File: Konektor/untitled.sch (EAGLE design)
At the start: 13 parts, among them J1 1744429-4, J2 1744429-4, J4 1744429-2, J5 1744429-2, J6 1744429-2, X1 MSTBA2, X2 MSTBA4, X3 MSTBA6, X6 MSTBA2, X7 C-GRID-02-70543, X8 MSTBA2

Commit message: PCB huawei
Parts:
- removed J4, J5, J6: 1744429-2, 1744429-2:1744429-2
- J1, J2: value 1744429-4 -> RJ45-8N-B; device 1744429-4:1744429-4 -> RJ45-8N-B:RJ45-8N-B
- X2: value MSTBA4 -> MSTBA5; device con-phoenix-508:MSTBA4 -> con-phoenix-508:MSTBA5
- X3: value MSTBA6 -> MSTBA5; device con-phoenix-508:MSTBA6 -> con-phoenix-508:MSTBA5
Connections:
- new net N$19: J1.8, J2.8
- new net N$20: J1.SHIELD, J2.SHIELD
- new net N$7: X2-5.1, X3-1.1
- new net N$8: J1.1, J2.1
- net N$10: now also J1.3, J2.3; no longer J4.2, X3-2.1
- net N$11: now also J1.4, J2.4; no longer J5.1, X3-3.1
- net N$12: now also J1.5, J2.5; no longer J5.2, X3-4.1
- net N$13: now also J1.6, J2.6; no longer J6.1, X3-5.1
- net N$14: now also J1.7, J2.7; no longer J6.2, X3-6.1
- net N$3: now also X3-5.1; no longer J1.1
- net N$4: now also X3-4.1; no longer J1.3
- net N$5: now also X3-3.1; no longer J2.1
- net N$6: now also X3-2.1; no longer J2.3
- net N$9: now also J1.2, J2.2; no longer J4.1, X3-1.1
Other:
- note removed: "ARUS R S T"
- note removed: "TEGANGAN 3 Phase"
- moved on the sheet: S1, X2-1, X2-2, X2-3, X2-4, X3-1, X3-2, X3-3, X3-4, X3-5, X6-1, X6-2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

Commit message: 3 PCB done
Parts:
- removed S1: DS01-254-L-04BE, DS01-254-L-04BE:DS01-254-L-04BE
- removed X3: MSTBA5, con-phoenix-508:MSTBA5
- removed X6, X8: MSTBA2, con-phoenix-508:MSTBA2
- removed X7: C-GRID-02-70543, con-molex:C-GRID-02-70543
- added DP-05RP1: (no value), DP-05RP:DP-05RP
- added EBYTEE220-900T22D1: (no value), EByte E220-900T22D:EBYTEE220-900T22D
- added KONEKTOR-3.81-13P1: (no value), KONEKTOR-3.81-13P:KONEKTOR-3.81-13P
- added R1: 10k, rcl:R-EU_R0805
- added RS1: C-GRID-02-70543, con-molex:C-GRID-02-70543
- added TTL-RS1: (no value), TTL-RS485:TTL-RS485
- X1: value MSTBA2 -> C-GRID-02-70543; device con-phoenix-508:MSTBA2 -> con-molex:C-GRID-02-70543
- X2: value MSTBA5 -> C-GRID-05-70543; device con-phoenix-508:MSTBA5 -> con-molex:C-GRID-05-70543
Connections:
- removed net A-LORA: S1.NO1, S1.NO3, X7-1.S
- removed net B-LORA: S1.NO2, S1.NO4, X7-2.S
- new net 5V: EBYTEE220-900T22D1.VCC, R1.2, RS485-1.S, TTL-RS1.VCC
- new net A: DP-05RP1.P$2, DP-05RP1.P$4, TTL-RS1.A
- new net A1: DP-05RP1.P$7, KONEKTOR-3.81-13P1.P$3
- new net B: DP-05RP1.P$3, DP-05RP1.P$5, TTL-RS1.B
- new net B1: DP-05RP1.P$8, KONEKTOR-3.81-13P1.P$4
- new net GND: DP-05RP1.P$6, EBYTEE220-900T22D1.GND, EBYTEE220-900T22D1.M0, RS485-2.S, TTL-RS1.GND
- new net M1: DP-05RP1.P$1, EBYTEE220-900T22D1.M1, R1.1
- net N$1: now also KONEKTOR-3.81-13P1.P$1, RS1-2.S; no longer RS485-1.S, X1-1.1
- net N$15: now also KONEKTOR-3.81-13P1.P$6, X2-4.S; no longer S1.COM1, X6-1.1
- net N$16: now also KONEKTOR-3.81-13P1.P$7, X2-3.S; no longer S1.COM2, X6-2.1
- net N$17: now also KONEKTOR-3.81-13P1.P$8, X2-2.S; no longer S1.COM3, X8-1.1
- net N$18: now also KONEKTOR-3.81-13P1.P$9, X2-1.S; no longer S1.COM4, X8-2.1
- net N$2: now also KONEKTOR-3.81-13P1.P$2, RS1-1.S; no longer RS485-2.S, X1-2.1
- net N$3: now also EBYTEE220-900T22D1.RXD, TTL-RS1.RX; no longer X2-1.1, X3-5.1
- net N$4: now also EBYTEE220-900T22D1.TXD, TTL-RS1.TX; no longer X2-2.1, X3-4.1
- net N$5: now also DP-05RP1.P$9, X1-1.S; no longer X2-3.1, X3-3.1
- net N$6: now also DP-05RP1.P$10, X1-2.S; no longer X2-4.1, X3-2.1
- net N$7: now also KONEKTOR-3.81-13P1.P$5, X2-5.S; no longer X2-5.1, X3-1.1
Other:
- note removed: "DIP-SWITCH"
- note removed: "RS485"
- moved on the sheet: J1, J2, RS485-1, RS485-2

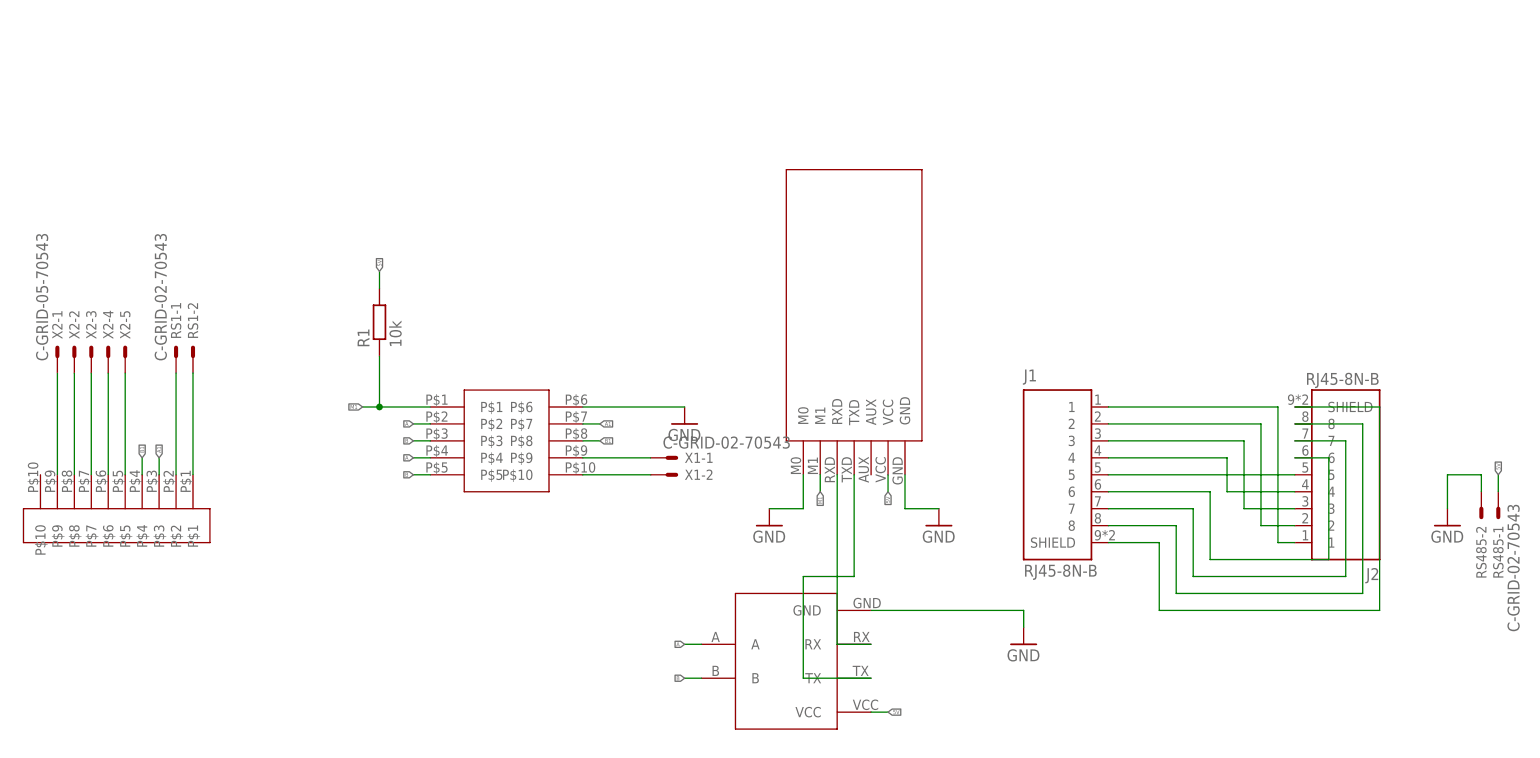
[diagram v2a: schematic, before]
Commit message: REVISI PCB Konektor
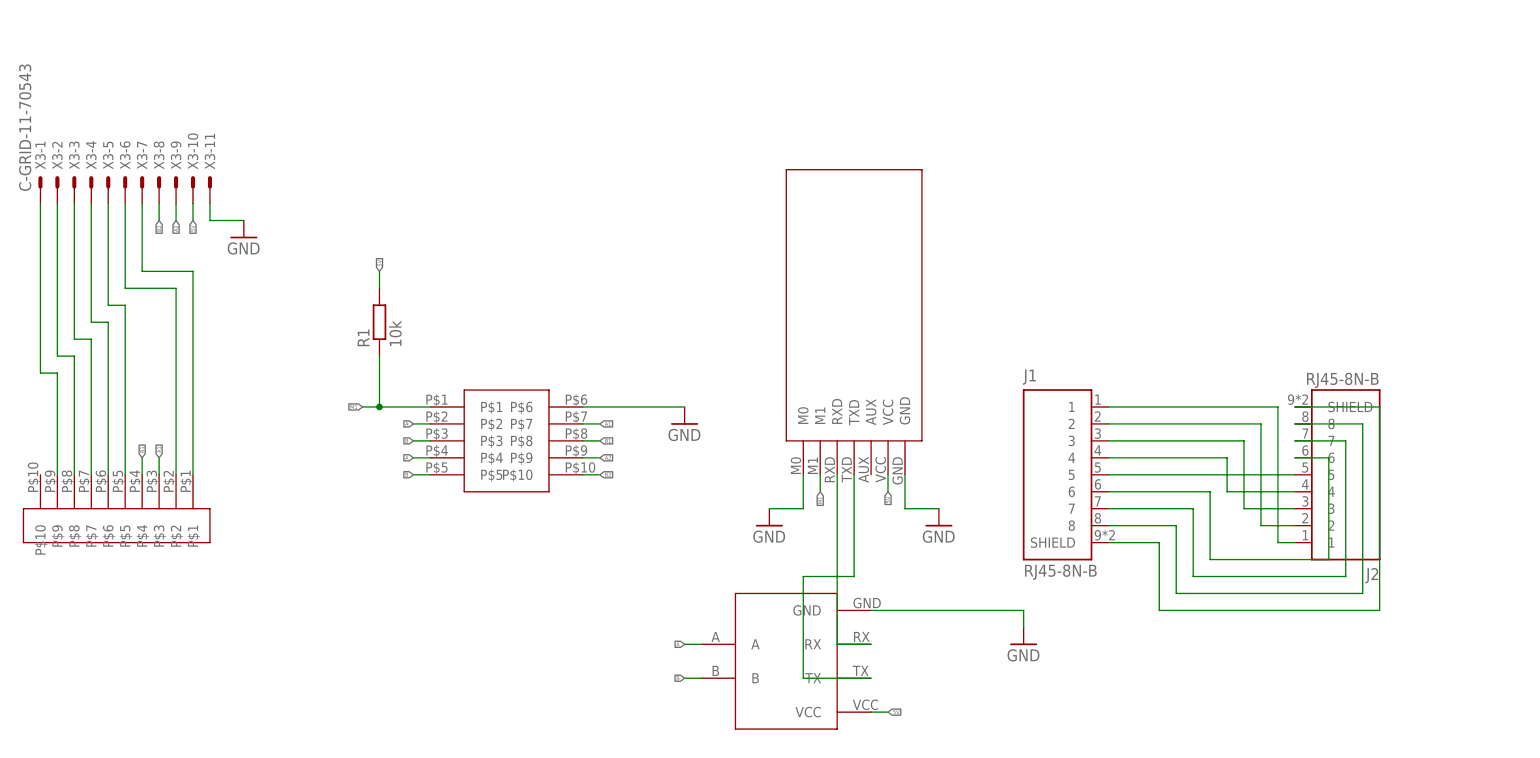
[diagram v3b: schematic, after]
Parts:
- removed RS1, RS485, X1: C-GRID-02-70543, con-molex:C-GRID-02-70543
- removed X2: C-GRID-05-70543, con-molex:C-GRID-05-70543
- added X3: C-GRID-11-70543, con-molex:C-GRID-11-70543
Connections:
- removed net N$5: DP-05RP1.P$9, X1-1.S
- removed net N$6: DP-05RP1.P$10, X1-2.S
- new net A2: DP-05RP1.P$9, X3-9.S
- new net B2: DP-05RP1.P$10, X3-8.S
- net 5V: now also X3-10.S; no longer RS485-1.S
- net GND: now also X3-11.S; no longer RS485-2.S
- net N$1: now also X3-7.S; no longer RS1-2.S
- net N$15: now also X3-4.S; no longer X2-4.S
- net N$16: now also X3-3.S; no longer X2-3.S
- net N$17: now also X3-2.S; no longer X2-2.S
- net N$18: now also X3-1.S; no longer X2-1.S
- net N$2: now also X3-6.S; no longer RS1-1.S
- net N$7: now also X3-5.S; no longer X2-5.S
